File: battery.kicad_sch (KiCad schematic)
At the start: 21 parts, among them IC1 FS312F-G, J1 USB_C_Receptacle, Q1 FS8205, SW3 SW_SPST, U8 TP4056, U9 MT3608

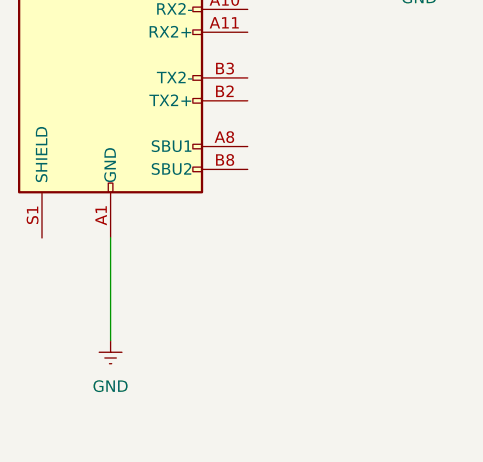
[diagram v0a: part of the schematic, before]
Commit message: feat: ground usb shield via 0k resistor
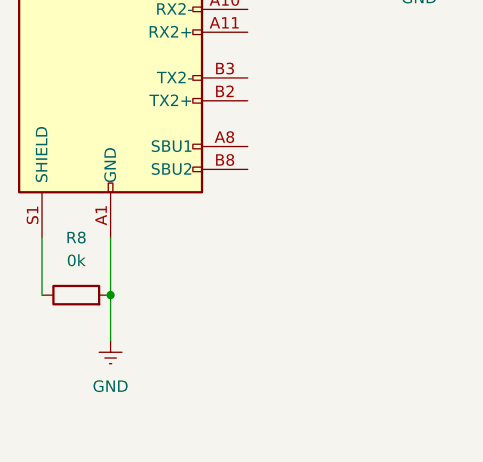
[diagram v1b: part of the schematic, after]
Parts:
- added R8: 0k, symbol Device:R
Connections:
- net GND: now also R8.2
- net at J1.S1 (SHIELD): now also R8.1
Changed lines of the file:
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@@
+	)
+	(junction
+		(at 44.45 104.14)
+		(diameter 0)
+		(color 0 0 0 0)
 	)
 	(junction
@@
 	(wire
 		(pts
+			(xy 36.83 97.79) (xy 36.83 104.14)
+		)
+		(stroke
+			(width 0)
+			(type default)
+		)
+	)
+	(wire
+		(pts
 			(xy 146.05 54.61) (xy 146.05 55.88)
 		)
@@
 	(wire
 		(pts
+			(xy 44.45 104.14) (xy 44.45 109.22)
+		)
+		(stroke
+			(width 0)
+			(type default)
+		)
+	)
+	(wire
+		(pts
 			(xy 105.41 48.26) (xy 99.06 48.26)
 		)
@@
 	(wire
 		(pts
-			(xy 44.45 97.79) (xy 44.45 109.22)
+			(xy 44.45 97.79) (xy 44.45 104.14)
 		)
 		(stroke
@@
 					(unit 1)
 				)
+			)
+		)
+	)
+	(symbol
+		(lib_id "Device:R")
+		(at 40.64 104.14 90)
+		(unit 1)
+		(exclude_from_sim no)
+		(in_bom yes)
+		(on_board yes)
+		(dnp no)
+		(fields_autoplaced yes)
+		(property "Reference" "R8"
+			(at 40.64 97.79 90)
+			(effects
+				(font
+					(size 1.27 1.27)
+				)
+			)
+		)
+		(property "Value" "0k"
+			(at 40.64 100.33 90)
+			(effects
+				(font
+					(size 1.27 1.27)
+				)
+			)
+		)
+		(property "Footprint" ""
+			(at 40.64 105.918 90)
+			(effects
+				(font
+					(size 1.27 1.27)
+				)
+				(hide yes)
+			)
+		)
+		(property "Datasheet" "~"
+			(at 40.64 104.14 0)
+			(effects
+				(font
+					(size 1.27 1.27)
+				)
+				(hide yes)
+			)
+		)
+		(property "Description" "Resistor"
+			(at 40.64 104.14 0)
+			(effects
+				(font
+					(size 1.27 1.27)
+				)
+				(hide yes)
+			)
+		)
+		(pin "2"
+		)
+		(pin "1"
+		)
+		(instances
+			(project "shadow"
+				(path "/3c2fce68-ba60-4bda-a294-ddd60ff77106/353b67ec-a1cb-4a2a-a9c5-6f61edaa503f"
+					(reference "R8")
+					(unit 1)
+				)

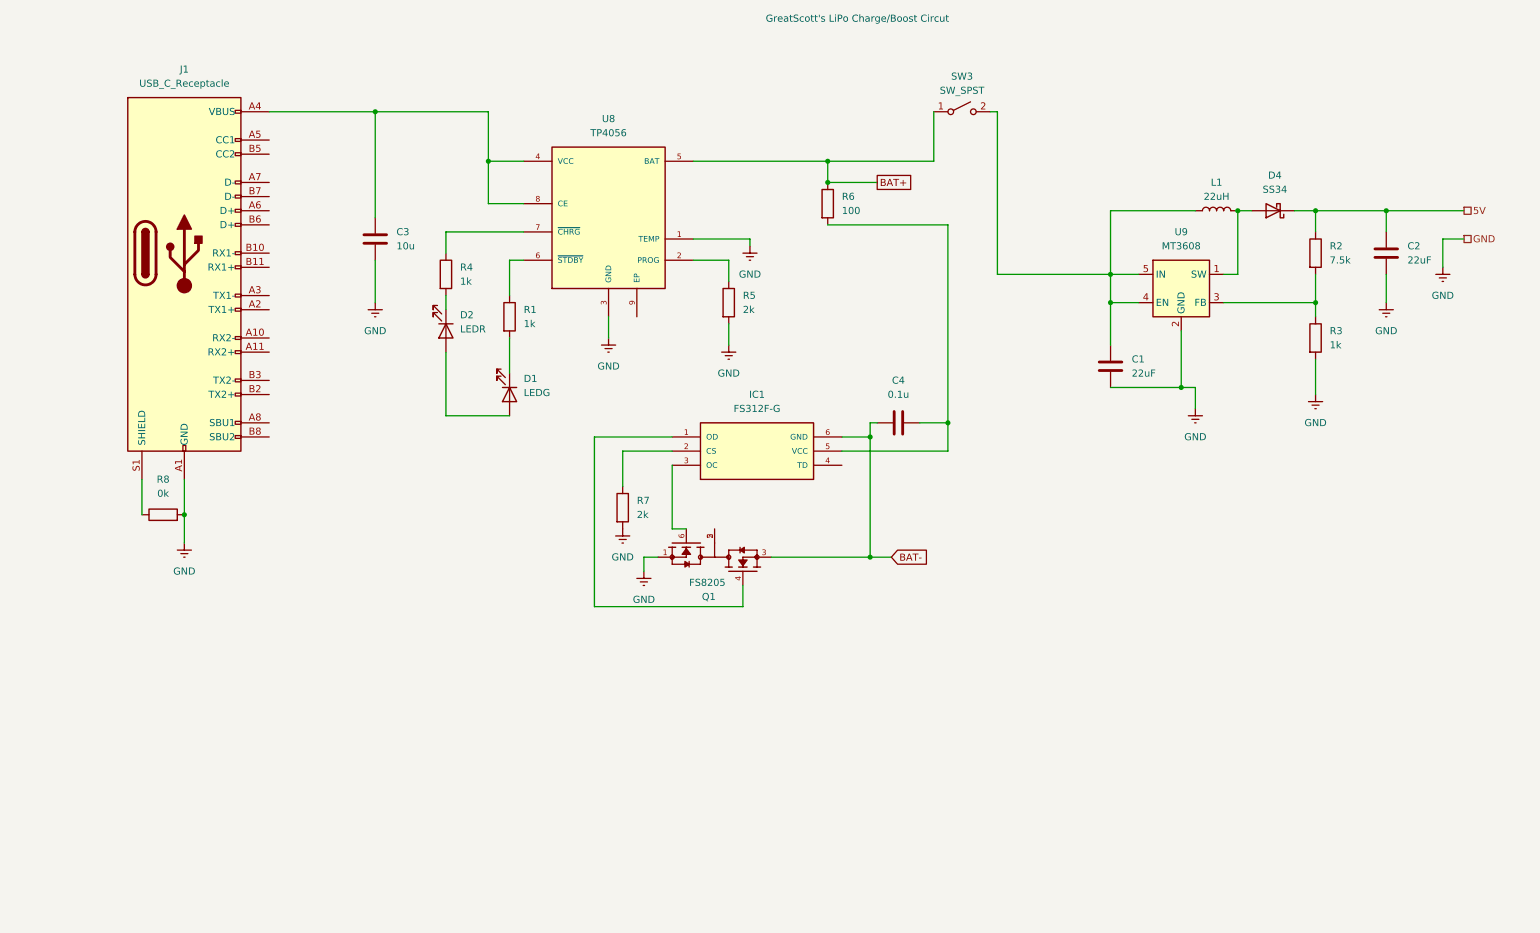
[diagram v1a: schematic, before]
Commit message: start work on i2c multiplexer
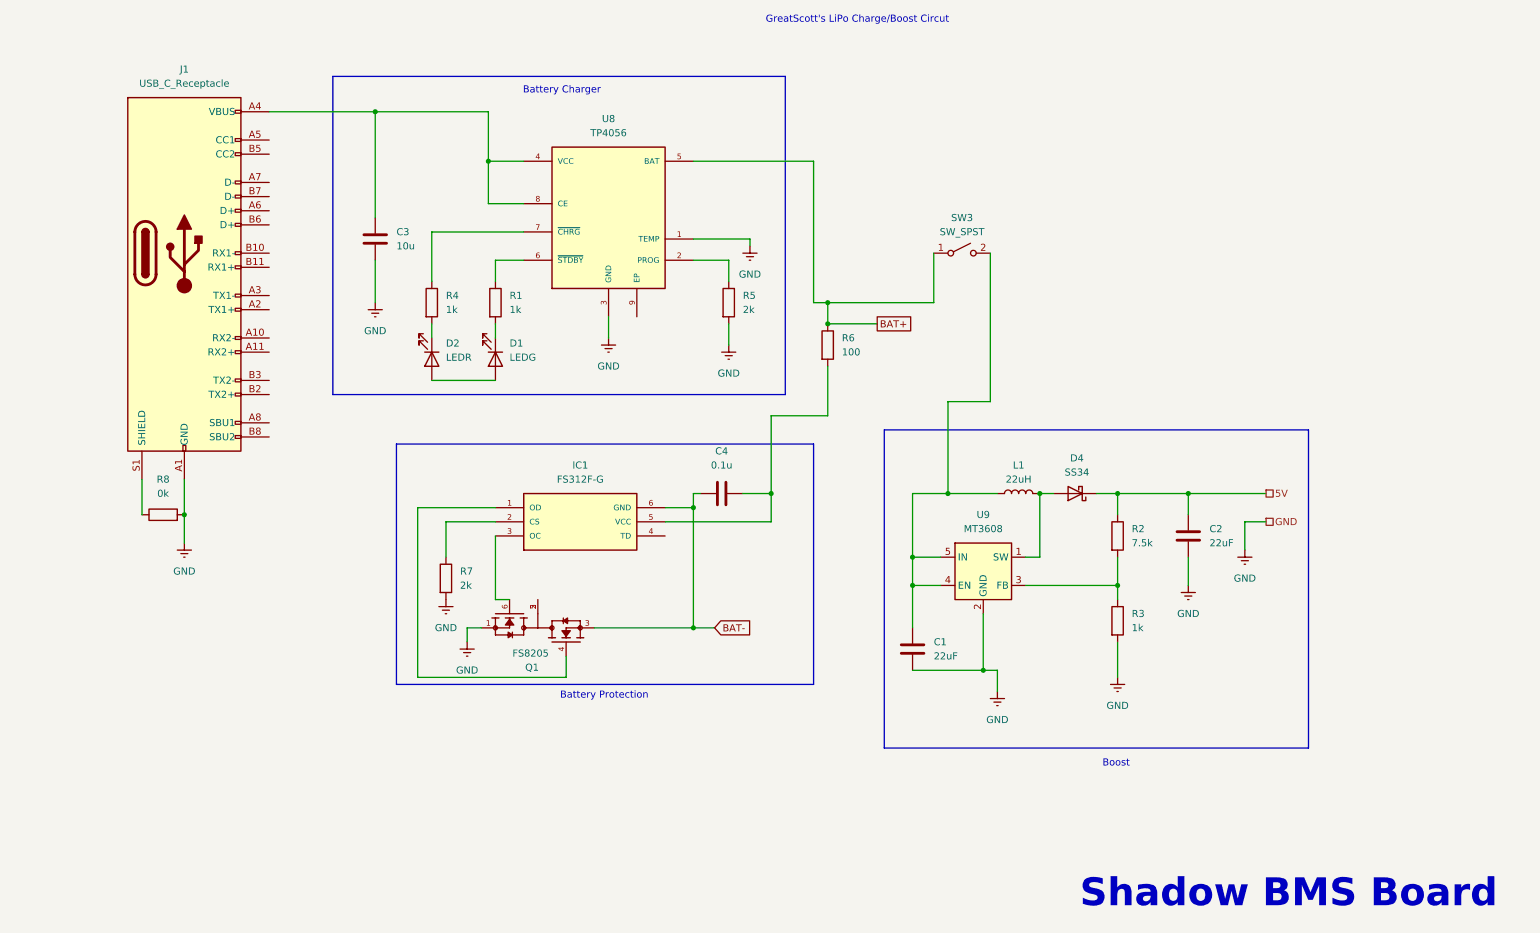
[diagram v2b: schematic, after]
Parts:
- R1, R2, R3, R4, R5, R6, R7, R8: footprint (none) -> Resistor_SMD:R_0201_0603Metric
- SW3: footprint (none) -> Button_Switch_THT:SW_DIP_SPSTx01_Slide_9.78x4.72mm_W7.62mm_P2.54mm
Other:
- note added: "Battery Charger"
- note added: "Battery Protection"
- note added: "Boost"
- note added: "Shadow BMS Board"
- moved on the sheet: C1, C2, C4, D1, D2, D4, IC1, L1, Q1, R1, R2, R3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

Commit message: switch to new (better) lipo charger design
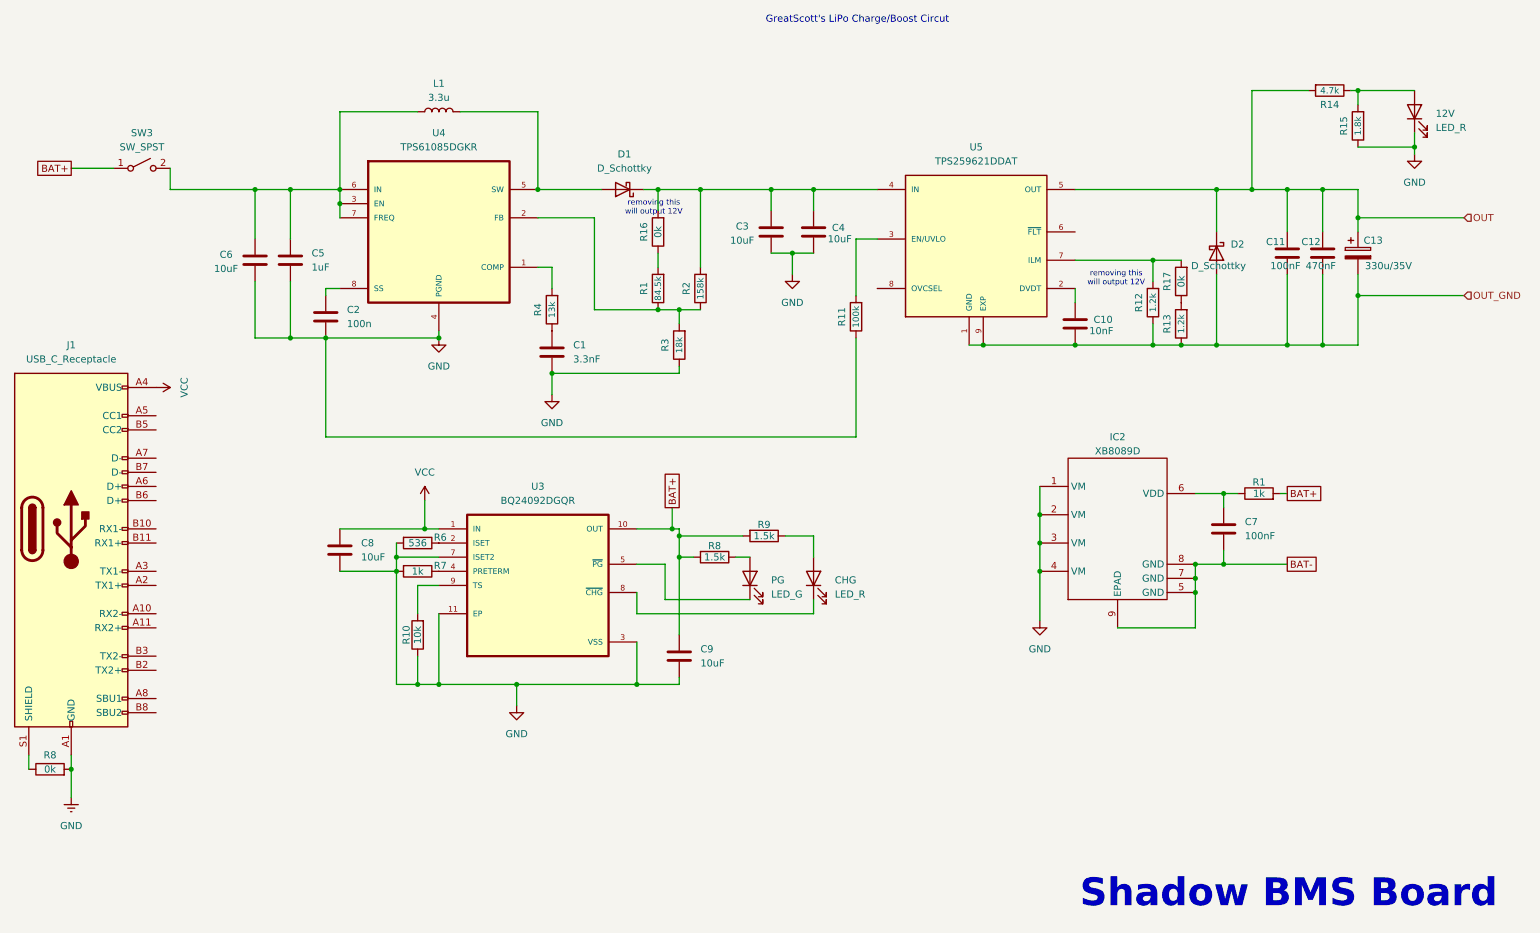
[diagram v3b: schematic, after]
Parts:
- removed D1: LEDG, LED_SMD:LED_0603_1608Metric, symbol Device:LED
- removed D2: LEDR, LED_SMD:LED_0603_1608Metric, symbol Device:LED
- removed D4: SS34, Diode_SMD:D_SMA, symbol Diode:SS34
- removed IC1: FS312F-G, FS312F-G:SOT23-6, symbol FS312F-G:FS312F-G
- removed Q1: FS8205, FS8205:SOT95P280X145-6N, symbol FS8205:FS8205
- removed R1: 1k, Resistor_SMD:R_0201_0603Metric, symbol Device:R
- removed R5: 2k, Resistor_SMD:R_0201_0603Metric, symbol Device:R
- removed U8: TP4056, TP4056:SOP127P600X175-9N, symbol TP4056:TP4056
- removed U9: MT3608, Package_TO_SOT_SMD:SOT-23-6, symbol Regulator_Switching:MT3608
- added 12V, CHG: LED_R, symbol Device:LED
- added C10: 10nF, symbol Device:C
- added C11, C7: 100nF, symbol Device:C
- added C12: 470nF, symbol Device:C
- added C13: 330u/35V, symbol Device:C_Polarized
- added C5: 1uF, symbol Device:C
- added C6, C8, C9: 10uF, symbol Device:C
- added D1, D2: D_Schottky, symbol Device:D_Schottky
- added IC2: XB8089D, ProLib_pcs_2025-01-25:SOIC-8_L5.0-W4.0-P1.27-LS6.0-BL-EP2.0, symbol ProLib_pcs_2025-01-25:XB8089D
- added PG: LED_G, symbol Device:LED
- added R1: 1k, symbol Device:R
- added R1: 84.5k, Resistor_SMD:R_0201_0603Metric, symbol Device:R
- added R10: 10k, symbol Device:R
- added R11: 100k, Resistor_SMD:R_0201_0603Metric, symbol Device:R
- added R12, R13: 1.2k, Resistor_SMD:R_0201_0603Metric, symbol Device:R
- added R14: 4.7k, Resistor_SMD:R_0201_0603Metric, symbol Device:R
- added R15: 1.8k, Resistor_SMD:R_0201_0603Metric, symbol Device:R
- added R16, R17: 0k, Resistor_SMD:R_0201_0603Metric, symbol Device:R
- added R8, R9: 1.5k, symbol Device:R
- added U3: BQ24092DGQR, BQ24092DGQR:IC_XTR111AIDGQR, symbol BQ24092DGQR:BQ24092DGQR
- added U4: TPS61085DGKR, TPS61085DGKR:SOP65P490X110-8N, symbol TPS61085DGKR:TPS61085DGKR
- added U5: TPS259621DDAT, TPS259621DDAT:IC_TPS259621DDAT, symbol TPS259621DDAT:TPS259621DDAT
- C1: value 22uF -> 3.3nF; footprint Capacitor_SMD:C_1812_4532Metric -> (none)
- C2: value 22uF -> 100n; footprint Capacitor_SMD:C_1812_4532Metric -> (none)
- C3: value 10u -> 10uF; footprint Capacitor_SMD:C_0201_0603Metric -> (none)
- C4: value 0.1u -> 10uF; footprint Capacitor_SMD:C_0201_0603Metric -> (none)
- L1: value 22uH -> 3.3u; footprint Inductor_SMD:L_1812_4532Metric -> (none)
- R2: value 7.5k -> 158k
- R3: value 1k -> 18k
- R4: value 1k -> 13k
- R6: value 100 -> 536; footprint Resistor_SMD:R_0201_0603Metric -> (none)
- R7: value 2k -> 1k; footprint Resistor_SMD:R_0201_0603Metric -> (none)
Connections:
- net BAT+: now also C9.1, R1.2, R8.2, R9.2, U3.10 (OUT); no longer R6.1
- net BAT-: now also C7.2, IC2.5 (GND), IC2.7 (GND), IC2.8 (GND), IC2.9 (EPAD); no longer C4.1
- net GND: now also C1.2, C2.2, C4.2, R3.1, R6.2, 12V.1 (K), C5.2, C6.2, C8.2, C9.2, IC2.1 (VM), IC2.2 (VM), IC2.3 (VM), IC2.4 (VM), R10.1, R11.1, R15.1, U3.11 (EP), U3.3 (VSS), U3.7 (ISET2), U4.4 (PGND); no longer C1.1, C2.1, R3.2
- net at L1.2: now also D1.2 (A), U4.5 (SW)
- net at R4.2: now also U4.1 (COMP)
- net VCC: now reaches J1.A4 (VBUS), J1.A9 (VBUS), J1.B4 (VBUS), J1.B9 (VBUS)
- net VCC: now also C8.1, U3.1 (IN); no longer C3.1
- net at R2.2: now also C3.1, C4.1, D1.1 (K), R16.2, U5.4 (IN); no longer R3.1
- net at L1.1, SW3.2 (B): now also C5.1, C6.1, U4.3 (EN), U4.6 (IN), U4.7 (FREQ); no longer C1.2
- net at R7.1: now also U3.4 (PRETERM)
- net at R4.1: now also C1.1
- net 5V: no longer names the net of R2.1
- net 5V: now also R3.2, R1.1, U4.2 (FB); no longer C2.2
- new net: C7.1, IC2.6 (VDD), R1.1
- new net: R13.2, R17.1
- new net: 12V.2 (A), R14.1, R15.2
- new net: CHG.2 (A), R9.1
- new net: CHG.1 (K), U3.8 (~{CHG})
- new net: R12.2, R17.2, U5.7 (ILM)
- new net: C2.1, U4.8 (SS)
- new net: PG.1 (K), U3.5 (~{PG})
- new net: PG.2 (A), R8.1
- new net: C10.1, U5.2 (DVDT)
- new net: R11.2, U5.3 (EN/UVLO)
- new net: R6.1, U3.2 (ISET)
- new net: R10.2, U3.9 (TS)
- new net: R1.2, R16.1
- new net OUT: C11.1, C12.1, C13.1, D2.1 (K), R14.2, U5.5 (OUT)
- new net OUT_GND: C10.2, C11.2, C12.2, C13.2, D2.2 (A), R12.1, R13.1, U5.1 (GND), U5.9 (EXP)
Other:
- note added: "removing this will output 12V"
- note removed: "Battery Charger"
- note removed: "Battery Protection"
- note removed: "Boost"
- moved on the sheet: J1, R8
